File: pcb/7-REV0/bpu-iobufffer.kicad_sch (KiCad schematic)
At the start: 37 parts, among them J301 Conn_01x10, J302 Conn_01x09, U301 AiP74LVC1T45GC363.TR, U302 AiP74LVC1T45GC363.TR, U303 AiP74LVC1T45GC363.TR, U304 AiP74LVC1T45GC363.TR, U305 AiP74LVC1T45GC363.TR, U306 AiP74LVC1T45GC363.TR, U307 AiP74LVC1T45GC363.TR, U308 AiP74LVC1T45GC363.TR

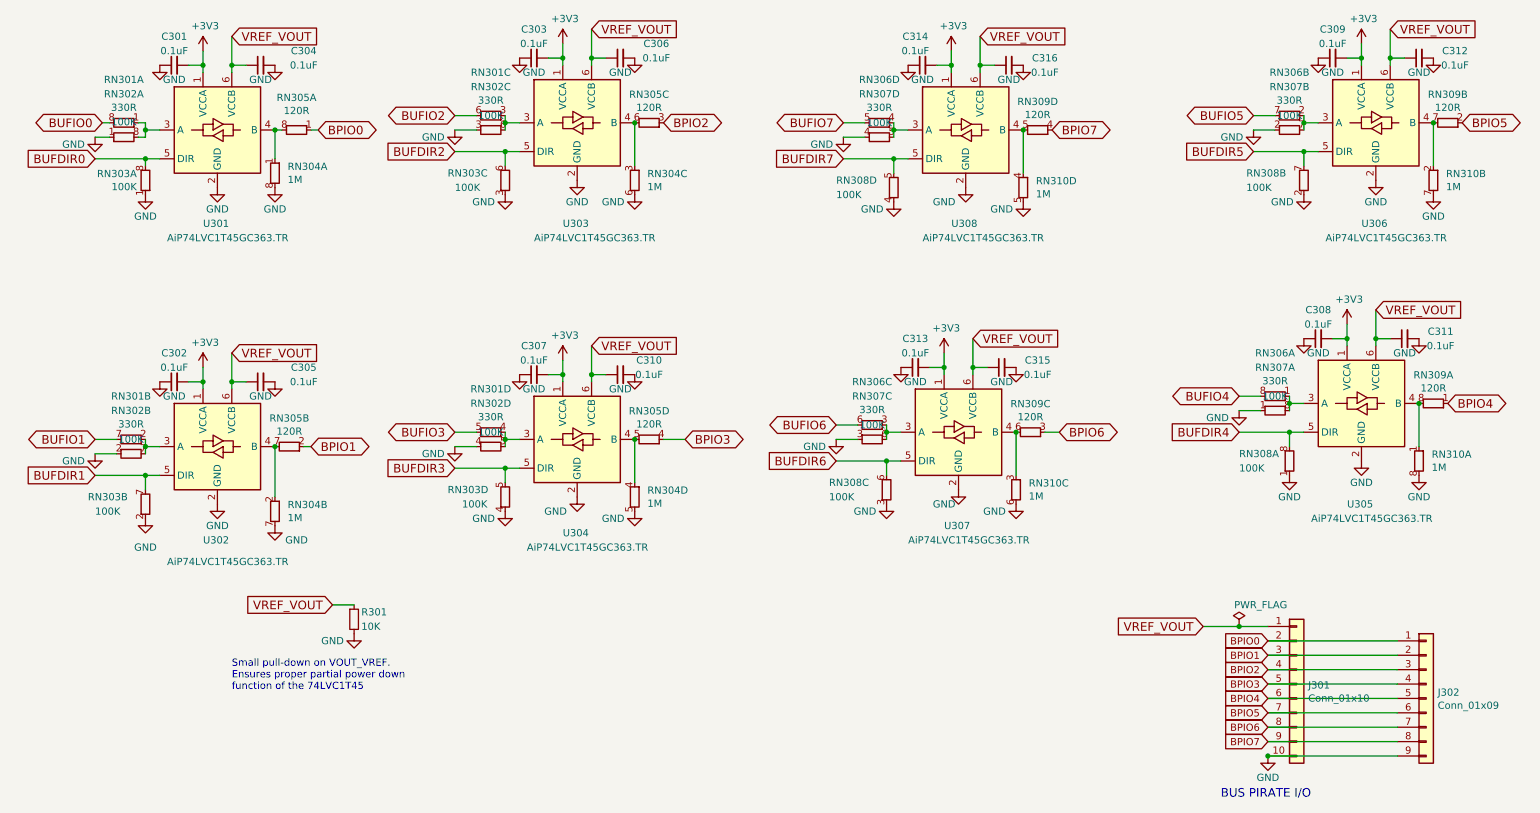
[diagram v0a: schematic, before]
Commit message: remove old pullups, remove 1M pull-down. Add footprints and updated PCB.
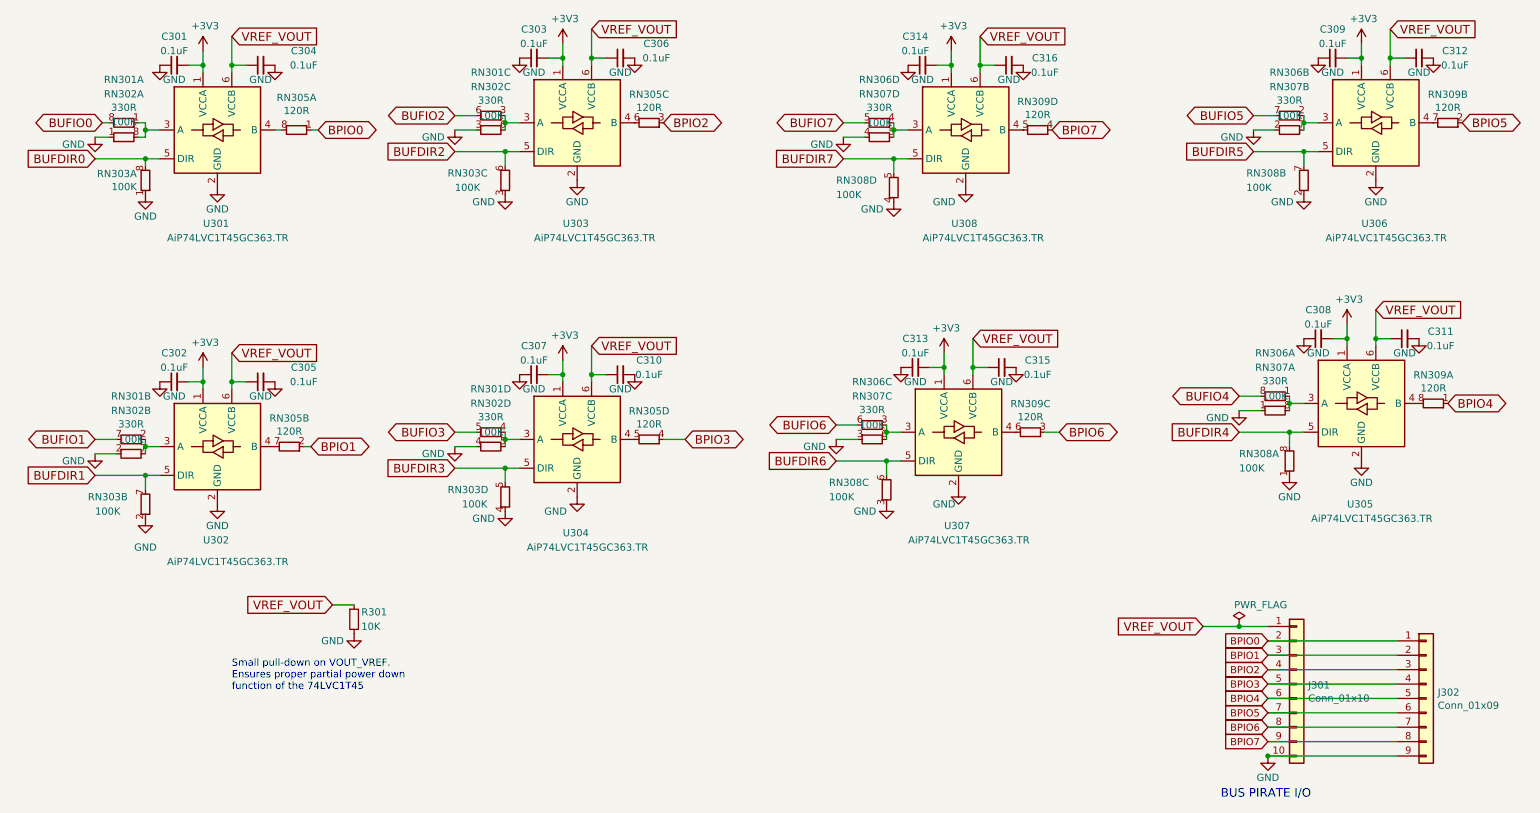
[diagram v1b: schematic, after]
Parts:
- removed RN304, RN310: 1M, Resistor_SMD:R_Array_Convex_4x0402, symbol dp-rarray:R_Array
